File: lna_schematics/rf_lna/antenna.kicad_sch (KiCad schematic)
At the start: 2 parts, among them J7 Conn_Coaxial_Small

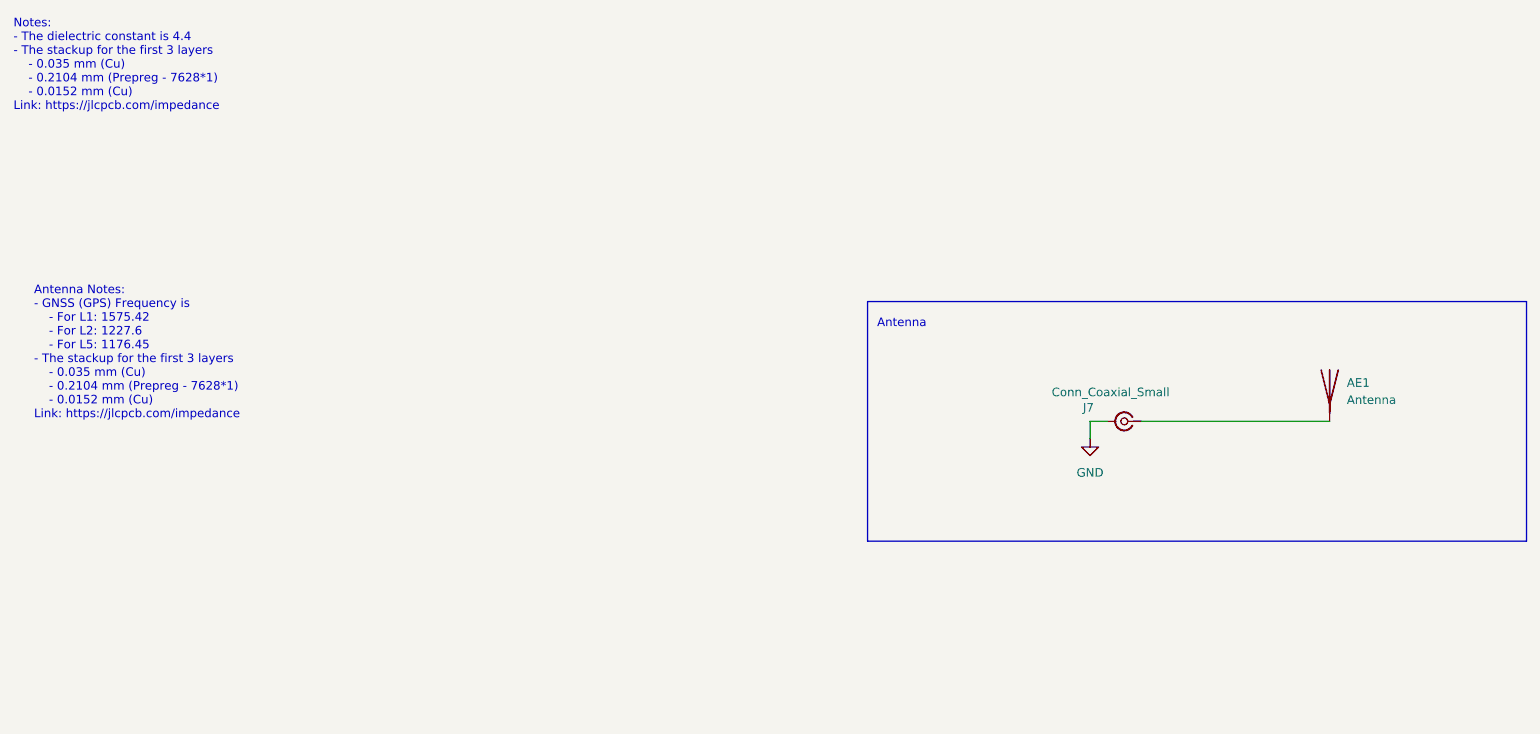
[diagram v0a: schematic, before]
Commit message: [kicad] Added antenna footprint to PCB | TODO: simulate and then add the antenna to the gerber as a whole
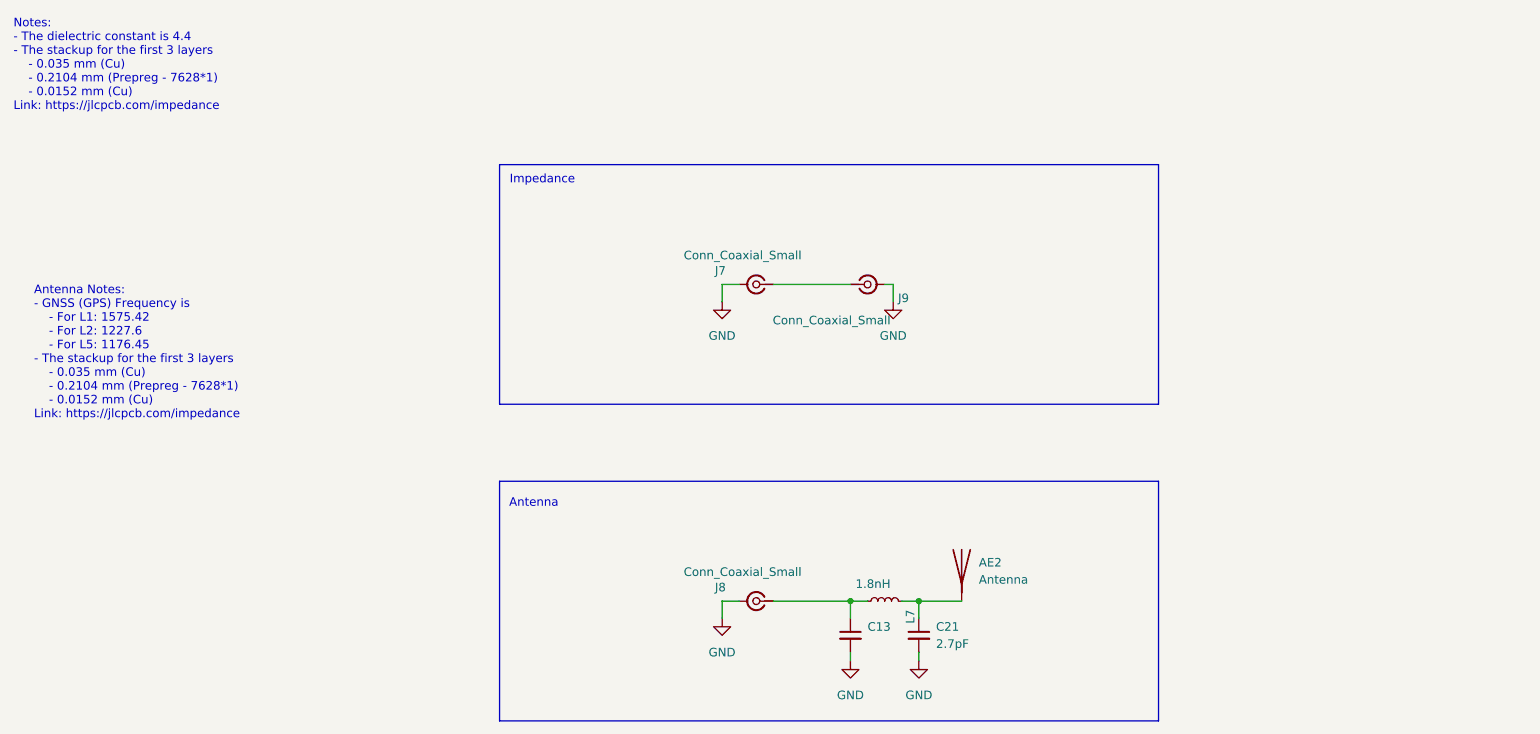
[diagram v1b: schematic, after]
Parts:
- removed AE1: Antenna, symbol Device:Antenna
- added AE2: Antenna, antennas:dn024, symbol Device:Antenna
- added C13: ~, Capacitor_SMD:C_0402_1005Metric, symbol Device:C_Small
- added C21: 2.7pF, Capacitor_SMD:C_0402_1005Metric, symbol Device:C_Small
- added J8, J9: Conn_Coaxial_Small, Library:SMA_Amphenol_901-143_Vertical, symbol Connector:Conn_Coaxial_Small
- added L7: 1.8nH, Inductor_SMD:L_0402_1005Metric, symbol Device:L_Small
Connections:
- net GND: now also C13.2, C21.2, J8.2 (Ext), J9.2 (Ext)
- net at J7.1 (In): now also J9.1 (In)
- new net: C13.1, J8.1 (In), L7.1
- new net: AE2.1 (A), C21.1, L7.2
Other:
- note added: "Impedance"
- moved on the sheet: J7
